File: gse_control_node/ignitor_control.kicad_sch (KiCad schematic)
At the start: 21 parts, among them J13 Conn_02x01, K2 G5Q-1 DC24, K3 G5Q-1 DC24, K4 G5Q-1 DC24, Q10 BSS138, Q4 BSS138, Q5 BSS138, U10 ACS713xLCTR-30A, U11 AMC3330

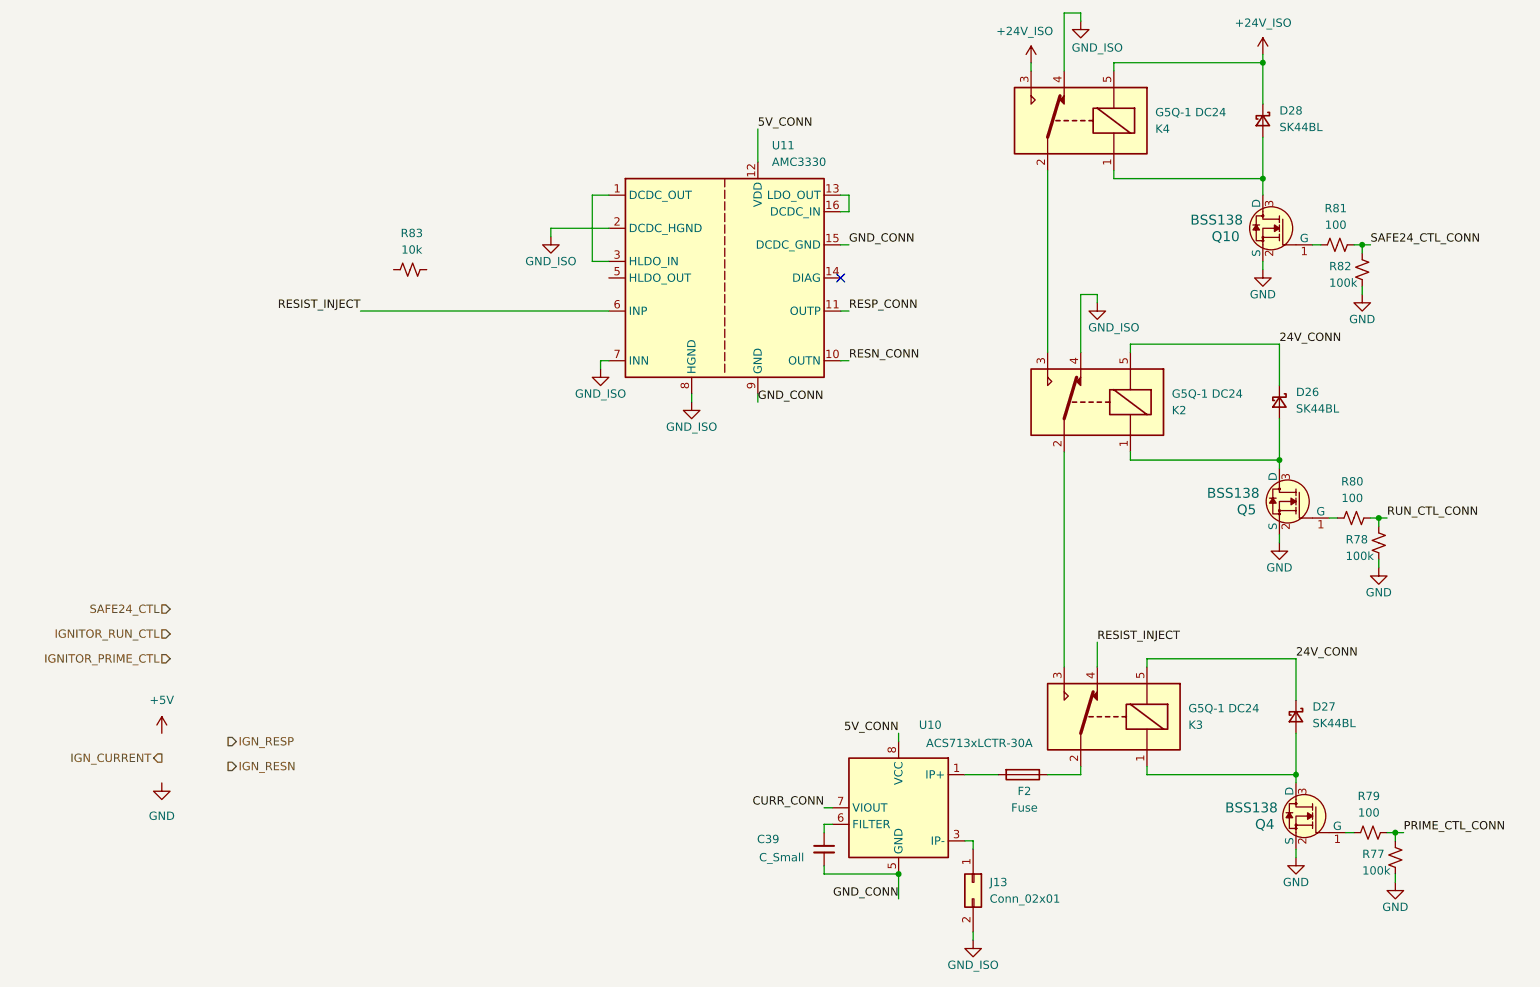
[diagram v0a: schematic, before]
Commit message: finish control board routing
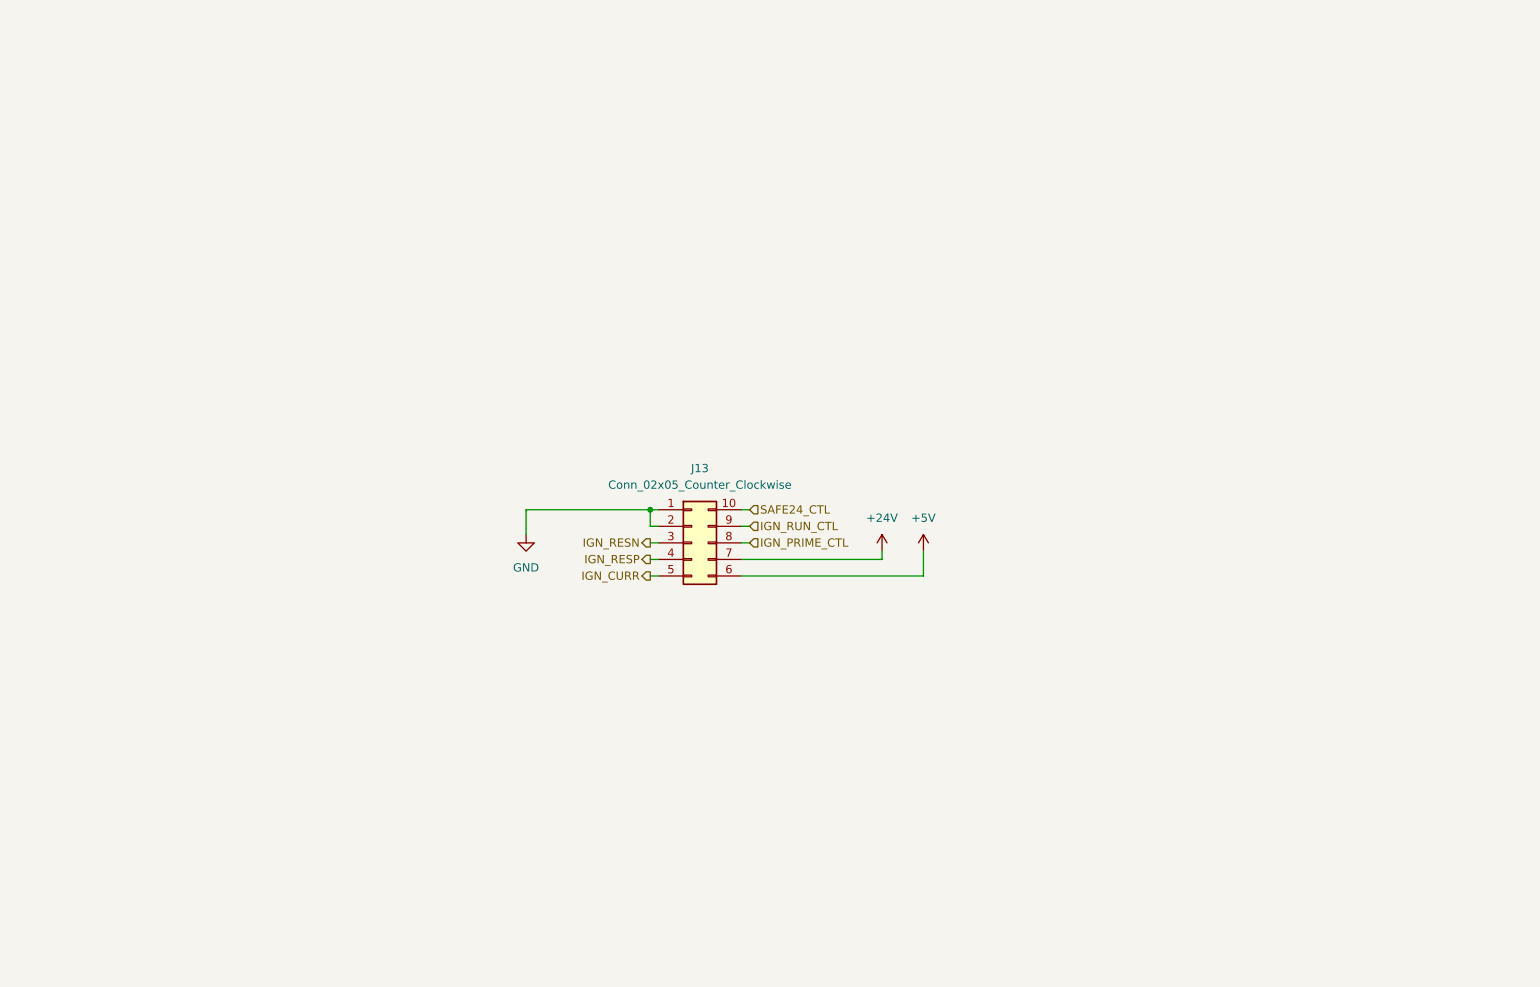
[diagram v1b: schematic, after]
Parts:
- removed C39: C_Small, symbol Device:C_Small
- removed D26, D27, D28: SK44BL, Diode_SMD:D_SMB, symbol Device:D_Schottky_Small
- removed F2: Fuse, Fuse:Fuseholder_Blade_Mini_Keystone_3568, symbol Device:Fuse
- removed J13: Conn_02x01, Connector_Molex:Molex_Mini-Fit_Jr_5566-02A_2x01_P4.20mm_Vertical, symbol Connector_Generic:Conn_02x01
- removed K2, K3, K4: G5Q-1 DC24, Relay_THT:Relay_SPDT_Omron-G5Q-1, symbol Relay:G5Q-1
- removed Q10, Q4, Q5: BSS138, Package_TO_SOT_SMD:SOT-23-3, symbol dk_Transistors-FETs-MOSFETs-Single:BSS138
- removed R77, R78, R82: 100k, Resistor_SMD:R_0402_1005Metric, symbol Device:R_Small_US
- removed R79, R80, R81: 100, Resistor_SMD:R_0402_1005Metric, symbol Device:R_Small_US
- removed R83: 10k, Resistor_SMD:R_0402_1005Metric, symbol Device:R_Small_US
- removed U10: ACS713xLCTR-30A, Package_SO:SOIC-8_3.9x4.9mm_P1.27mm, symbol Sensor_Current:ACS713xLCTR-30A
- removed U11: AMC3330, Package_SO:SOIC-16W_7.5x10.3mm_P1.27mm, symbol Isolator_Analog:AMC3330
- added J13: Conn_02x05_Counter_Clockwise, Connector_Molex:Molex_Micro-Fit_3.0_43045-1012_2x05_P3.00mm_Vertical, symbol Connector_Generic:Conn_02x05_Counter_Clockwise
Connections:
- net +5V: now also J13.6 (Pin_6)
- net GND: now also J13.1 (Pin_1), J13.2 (Pin_2)
- net IGN_RESN: now also J13.3 (Pin_3)
- net IGN_RESP: now also J13.4 (Pin_4)
- net SAFE24_CTL: now also J13.10 (Pin_10)
- new net +24V: J13.7 (Pin_7)
- new net IGN_CURR: J13.5 (Pin_5)
- new net IGN_PRIME_CTL: J13.8 (Pin_8)
- new net IGN_RUN_CTL: J13.9 (Pin_9)
- no-connect marks 1 -> 0
